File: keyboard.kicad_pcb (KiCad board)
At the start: 2 copper layers, 285 x 94.6 mm, 256 parts, among them J1 USB_B_Micro, J2 JST_PH, J3 JST_PH, J4 Conn_ARM_JTAG_SWD_10, J5 Conn_01x10, Q1 Q_NMOS, SW1 SSSS912000, U1 BQ21040, U2 BL652, U3 TLV70033, Y1 32.768kHz

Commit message: I think we are ready
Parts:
- removed the R3 at (67.3, 134.8)
- added R3: R, Resistor_THT:R_Axial_DIN0207_L6.3mm_D2.5mm_P10.16mm_Horizontal, B.Cu at (64.8, 135.9)
- added R3: R_1206_3216Metric, Resistor_SMD:R_1206_3216Metric, B.Cu at (64.8, 141.0)
- R2: footprint Capacitor_SMD:C_0603_1608Metric -> Resistor_SMD:R_0603_1608Metric
- R4: value 10k -> 100k
- moved LED1 0.25 mm to (85.9, 66.8), turned to 270 degrees
- moved R7 0.25 mm to (87.6, 66.8), turned to 270 degrees
- renumbered LED102 to LED101, LED103 to LED102, LED104 to LED103, LED105 to LED104, LED106 to LED105, LED107 to LED106, LED108 to LED107, LED109 to LED108, LED110 to LED109, LED111 to LED110, LED112 to LED111, LED113 to LED112, LED114 to LED113, LED115 to LED114, LED116 to LED115, LED117 to LED116, LED118 to LED117, LED119 to LED118, LED120 to LED119, LED121 to LED120, LED122 to LED121, LED123 to LED122, LED124 to LED123, LED125 to LED124, LED126 to LED125, LED127 to LED126, LED128 to LED127, LED129 to LED128, LED130 to LED129, LED131 to LED130, LED132 to LED131, LED133 to LED132, LED134 to LED133, LED135 to LED134, LED136 to LED135, LED137 to LED136, LED138 to LED137, LED139 to LED138, LED140 to LED139, LED141 to LED140, LED142 to LED141, LED143 to LED142, LED144 to LED143, LED145 to LED144, LED146 to LED145, LED147 to LED146, LED148 to LED147, LED149 to LED148, LED150 to LED149, LED151 to LED150, LED152 to LED151, LED153 to LED152, LED154 to LED153, LED155 to LED154, LED156 to LED155, LED157 to LED156, LED158 to LED157, LED159 to LED158, LED160 to LED159, LED161 to LED160, LED162 to LED161, LED163 to LED162, LED164 to LED163, LED165 to LED164, LED166 to LED165, LED167 to LED166, LED168 to LED167, LED169 to LED168, LED170 to LED169, LED171 to LED170, LED172 to LED171, LED173 to LED172, LED174 to LED173, LED175 to LED174, LED176 to LED175, LED177 to LED176, LED178 to LED177, LED179 to LED178, LED180 to LED179, LED181 to LED180, LED182 to LED181, LED183 to LED182, LED184 to LED183, LED185 to LED184, LED101 to LED2
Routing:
- net +3V3: track 233.5 -> 240.8 mm
- net /Leds/LED+: track 1448.7 -> 1455.4 mm
- net /VBUS: track 268.8 -> 267.7 mm
- net /NCHG: track 277.9 -> 279.0 mm

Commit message: Final touchups
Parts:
- added G***: LOGO, logos:cc-by-sa, B.Cu at (141.0, 149.9)
- added REF**: OSHW-Logo2_7.3x6mm_SilkScreen, Symbol:OSHW-Logo2_7.3x6mm_SilkScreen, B.Cu at (152.4, 149.9)
- moved R4 3.78 mm to (86.4, 100.3), turned to 270 degrees
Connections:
- J1 pad 6: Net-(J1-Pad6) -> GND
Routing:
- net GND: track 189.3 -> 17.7 mm, vias 59 -> 62
- net /Leds/LED+: track 1455.4 -> 1447.5 mm
- net /VBUS: track 267.7 -> 263.0 mm, vias 2 -> 3
- net /VBAT_SENSE: track 101.3 -> 97.1 mm
- net /row4: track 282.2 -> 285.1 mm
- net Net-(D116-Pad2): track 31.2 -> 34.1 mm
- net /BKLT_LED: track 112.6 -> 114.6 mm
- net /row5: track 545.1 -> 543.5 mm
- net /row3: track 322.0 -> 321.0 mm
- net /Leds/LED-: track 1432.2 -> 1431.4 mm, vias 12 -> 13
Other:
- board text added: "BLU60"
- board text added: "Based on GH60 by komar007 & jdcarpe"
- board text added: "D+"
- board text added: "D-"
- board text added: "Designed by Andrew Chen"
- board text added: "v0.1"

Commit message: Really final touchups
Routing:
- net /Leds/LED-: track 1431.4 -> 1432.0 mm
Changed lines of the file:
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@@
     (thickness 1.6)
     (drawings 294)
-    (tracks 1617)
+    (tracks 1618)
     (zones 0)
     (modules 259)
@@
       (plotinvisibletext false)
       (padsonsilk true)
-      (subtractmaskfromsilk false)
+      (subtractmaskfromsilk true)
       (outputformat 1)
       (mirror false)
@@
   (segment (start 327.3552 70.104) (end 335.50225 70.104) (width 0.4064) (layer F.Cu) (net 102))
   (segment (start 90.58275 70.104) (end 89.2175 68.73875) (width 0.4064) (layer F.Cu) (net 102) (status 20))
-  (segment (start 320.89725 87.78875) (end 319.532 89.154) (width 0.4064) (layer F.Cu) (net 102))
-  (segment (start 332.105 87.78875) (end 320.89725 87.78875) (width 0.4064) (layer F.Cu) (net 102) (status 10))
   (segment (start 98.7425 89.1413) (end 98.7552 89.154) (width 0.4064) (layer F.Cu) (net 102))
   (segment (start 98.7425 87.78875) (end 98.7425 89.1413) (width 0.4064) (layer F.Cu) (net 102) (status 10))
@@
   (segment (start 308.2925 89.1413) (end 308.3052 89.154) (width 0.4064) (layer F.Cu) (net 102))
   (segment (start 308.2925 87.78875) (end 308.2925 89.1413) (width 0.4064) (layer F.Cu) (net 102) (status 10))
-  (segment (start 319.532 89.154) (end 308.3052 89.154) (width 0.4064) (layer F.Cu) (net 102))
   (segment (start 308.3052 89.154) (end 289.2552 89.154) (width 0.4064) (layer F.Cu) (net 102))
   (segment (start 74.93 87.78875) (end 74.93635 87.78875) (width 0.4064) (layer F.Cu) (net 102) (status 30))
@@
   (segment (start 88.392 126.492) (end 88.392 127.254) (width 0.4064) (layer F.Cu) (net 102))
   (segment (start 88.392 108.966) (end 88.392 108.204) (width 0.4064) (layer F.Cu) (net 102))
+  (segment (start 313.436 87.122) (end 311.404 89.154) (width 0.4064) (layer F.Cu) (net 102))
+  (segment (start 331.43825 87.122) (end 313.436 87.122) (width 0.4064) (layer F.Cu) (net 102))
+  (segment (start 311.404 89.154) (end 308.3052 89.154) (width 0.4064) (layer F.Cu) (net 102))
+  (segment (start 332.105 87.78875) (end 331.43825 87.122) (width 0.4064) (layer F.Cu) (net 102))
   (segment (start 164.5796 148.73) (end 165.28 148.73) (width 0.2032) (layer B.Cu) (net 103) (status 20))
   (segment (start 164.3888 148.5392) (end 164.5796 148.73) (width 0.2032) (layer B.Cu) (net 103))

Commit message: Fixing up my stupid mistake
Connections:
- J4 pad 2: /SWDCLK -> /SWDIO
- J4 pad 4: /SWDIO -> /SWDCLK
- J5 pad 1: /SWDIO -> /SWDCLK
- J5 pad 2: /SWDCLK -> /SWDIO
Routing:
- net /row5: track 543.5 -> 544.2 mm
- net Net-(D113-Pad1): track 31.1 -> 30.4 mm
- net Net-(D111-Pad1): track 16.3 -> 16.9 mm
- net GND: vias 62 -> 58
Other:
- net class LED added: clearance 0.2032, trace_width 0.4064, via_dia 0.6, via_drill 0.4
- net class POWER: trace_width 0.4064 -> 0.6096
- board text added: "DIO"
- board text added: "Expansion"
- board text removed: "SWDIO"

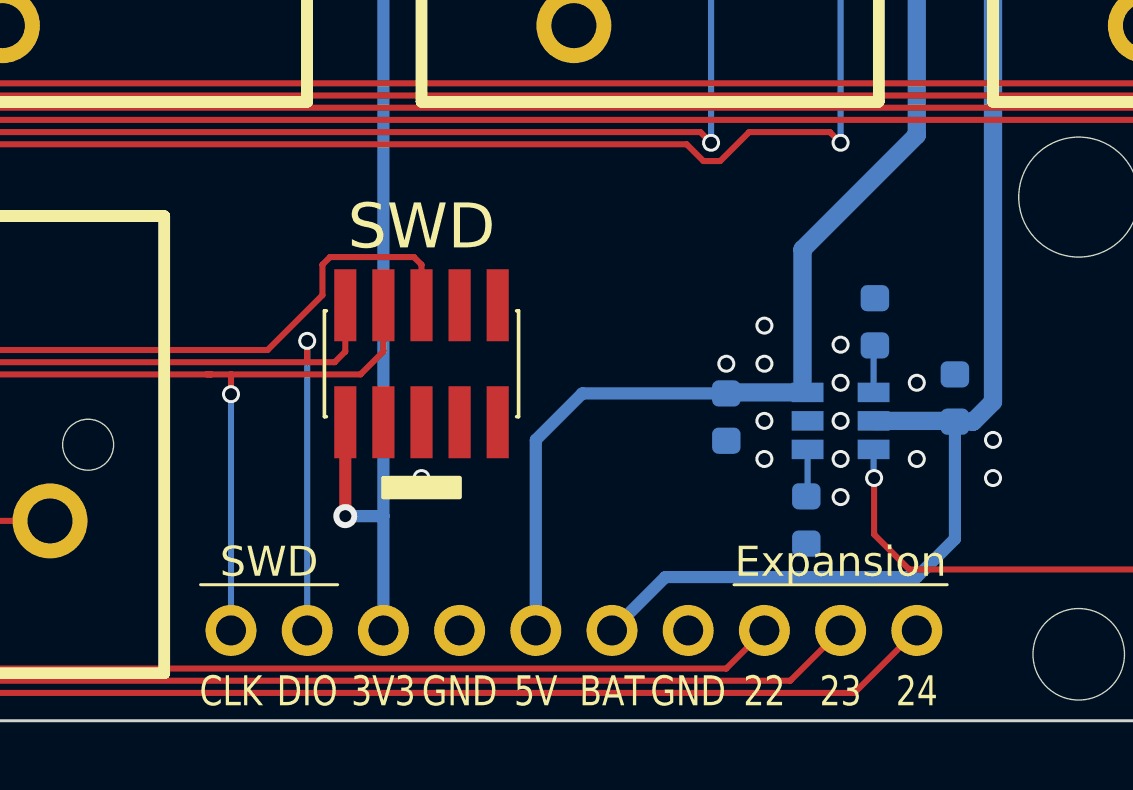
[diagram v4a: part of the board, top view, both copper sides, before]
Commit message: Silkscreen changes
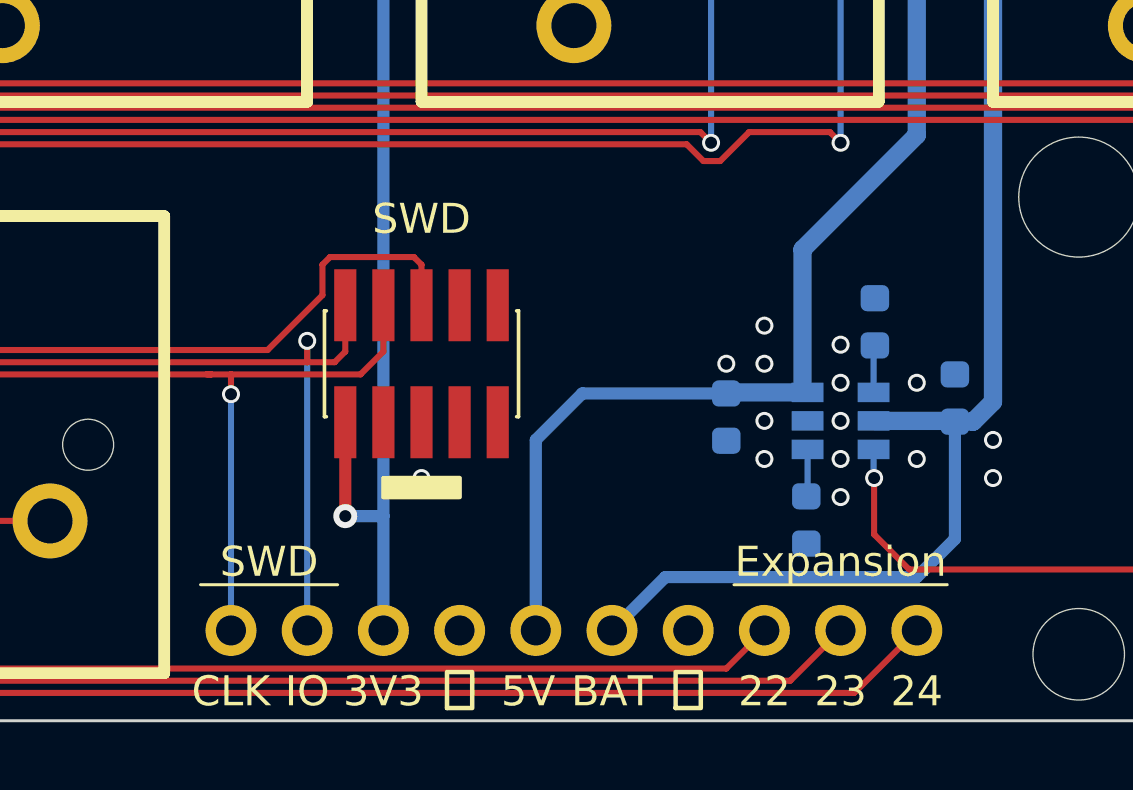
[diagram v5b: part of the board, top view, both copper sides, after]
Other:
- board text added: "IO"
- board text added: "⏚"
- board text removed: "DIO"
- board text removed: "GND"
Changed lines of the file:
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@@
   )
   (gr_text 24 (at 237.49 158.242) (layer F.SilkS)
-    (effects (font (size 1 0.8) (thickness 0.15)))
+    (effects (font (size 1 1) (thickness 0.15)))
   )
   (gr_text 23 (at 234.95 158.242) (layer F.SilkS)
-    (effects (font (size 1 0.8) (thickness 0.15)))
+    (effects (font (size 1 1) (thickness 0.15)))
   )
   (gr_text 22 (at 232.41 158.242) (layer F.SilkS)
-    (effects (font (size 1 0.8) (thickness 0.15)))
+    (effects (font (size 1 1) (thickness 0.15)))
   )
   (gr_text - (at 99.06 101.346 180) (layer B.SilkS)
@@
     (effects (font (size 2.032 1.524) (thickness 0.3048)) (justify mirror))
   )
-  (gr_text SWD (at 220.98 142.748) (layer F.SilkS)
-    (effects (font (size 1.5 1.5) (thickness 0.2)))
-  )
-  (gr_text "GND\n" (at 229.87 158.242) (layer F.SilkS)
-    (effects (font (size 1 0.8) (thickness 0.15)))
-  )
-  (gr_text 5V (at 224.79 158.242) (layer F.SilkS)
-    (effects (font (size 1 0.8) (thickness 0.15)))
+  (gr_text SWD (at 220.98 142.494) (layer F.SilkS)
+    (effects (font (size 1 1) (thickness 0.15)))
+  )
+  (gr_text ⏚ (at 229.87 158.242) (layer F.SilkS)
+    (effects (font (size 1.2 1.2) (thickness 0.15)))
+  )
+  (gr_text 5V (at 224.536 158.242) (layer F.SilkS)
+    (effects (font (size 1 1) (thickness 0.15)))
   )
   (gr_text BAT (at 227.33 158.242) (layer F.SilkS)
-    (effects (font (size 1 0.8) (thickness 0.15)))
-  )
-  (gr_text DIO (at 217.17 158.242) (layer F.SilkS)
-    (effects (font (size 1 0.8) (thickness 0.15)))
-  )
-  (gr_text "GND\n" (at 222.25 158.242) (layer F.SilkS)
-    (effects (font (size 1 0.8) (thickness 0.15)))
+    (effects (font (size 1 1) (thickness 0.15)))
+  )
+  (gr_text IO (at 217.17 158.242) (layer F.SilkS)
+    (effects (font (size 1 1) (thickness 0.15)))
+  )
+  (gr_text ⏚ (at 222.25 158.242) (layer F.SilkS)
+    (effects (font (size 1.2 1.2) (thickness 0.15)))
   )
   (gr_text 3V3 (at 219.71 158.242) (layer F.SilkS)
-    (effects (font (size 1 0.8) (thickness 0.15)))
+    (effects (font (size 1 1) (thickness 0.15)))
   )
   (gr_text "CLK\n" (at 214.63 158.242) (layer F.SilkS)
-    (effects (font (size 1 0.8) (thickness 0.15)))
+    (effects (font (size 1 1) (thickness 0.15)))
   )
   (gr_text + (at 213.36 103.378) (layer B.SilkS)
@@
   (gr_line (start 275.5011 140.12672) (end 275.5011 159.12592) (angle 90) (layer Dwgs.User) (width 0.381))
   (gr_line (start 251.74956 140.12672) (end 251.74956 159.12592) (angle 90) (layer Dwgs.User) (width 0.381))
-  (via (at 180.34 153.1112) (size 0.6) (drill 0.4) (layers F.Cu B.Cu) (net 28))
   (segment (start 202.5904 146.4564) (end 185.42 146.4564) (width 0.2032) (layer F.Cu) (net 1))
   (via (at 234.95 149.225) (size 0.6) (drill 0.4) (layers F.Cu B.Cu) (net 1))
@@
   (segment (start 67.056 92.5068) (end 68.072 91.4908) (width 0.2032) (layer F.Cu) (net 27))
   (segment (start 68.072 84.328) (end 68.072 91.4908) (width 0.2032) (layer F.Cu) (net 27))
+  (via (at 180.34 153.1112) (size 0.6) (drill 0.4) (layers F.Cu B.Cu) (net 28))
   (segment (start 219.71 146.9136) (end 219.71 145.37) (width 0.2032) (layer F.Cu) (net 28) (status 20))
   (segment (start 218.948 147.6756) (end 219.71 146.9136) (width 0.2032) (layer F.Cu) (net 28))

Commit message: mechanical changes
- moved micro usb connector up 1.1mm
- made micro usb pads 1mm longer
- changed mounting hole drill from 2.5mm to 2mm
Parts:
- J1: footprint Connector_USB:USB_Micro-B_Molex-105017-0001 -> usb:USB_Micro-B_Molex-105017-0001
- moved J1 1.10 mm to (80.5, 66.2)
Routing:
- net /VBUS: track 263.0 -> 263.7 mm
- net /USB_D-: track 179.6 -> 180.3 mm
- net /USB_D+: track 178.3 -> 179.0 mm

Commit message: tweaked thermal reliefs
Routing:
- net GND: track 17.7 -> 29.0 mm
